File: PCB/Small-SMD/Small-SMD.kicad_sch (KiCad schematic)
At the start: 24 parts, among them J1 Daisy port in, J3 UART, J4 Daisy port out, K1 HYC77-TF09-200, U1 PC817C-S, U2 SE5218, U21 TXB0104QPWRQ1

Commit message: Switch to cheaper IDC box header
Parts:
- J1: LCSC C305958 -> C3405
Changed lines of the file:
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@@
 			)
 		)
-		(property "LCSC" "C305958"
+		(property "LCSC" "C3405"
 			(at 129.54 36.83 0)
 			(effects

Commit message: Fix D2
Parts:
- D2: LCSC C258170 -> C167101
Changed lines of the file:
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@@
 			)
 		)
-		(property "LCSC" "C258170"
+		(property "LCSC" "C167101"
 			(at 168.91 49.53 90)
 			(effects

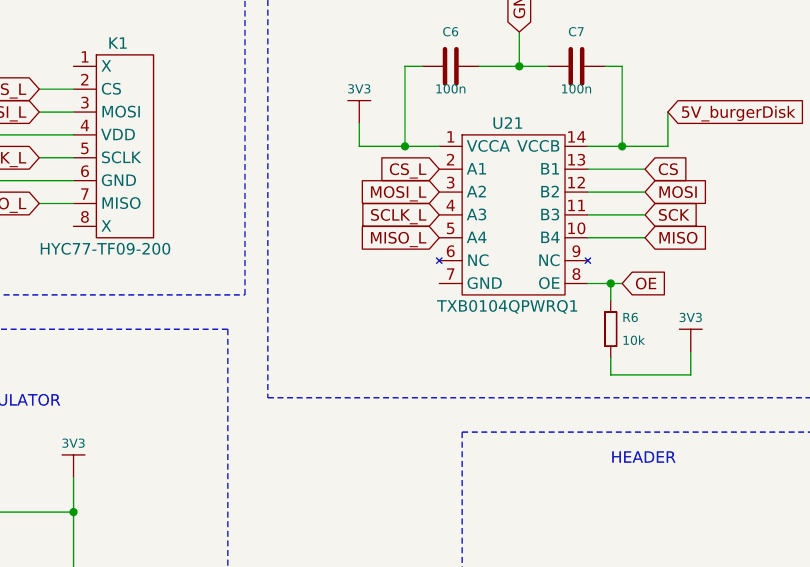
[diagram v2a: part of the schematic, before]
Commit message: Add GND to level shifter :-/
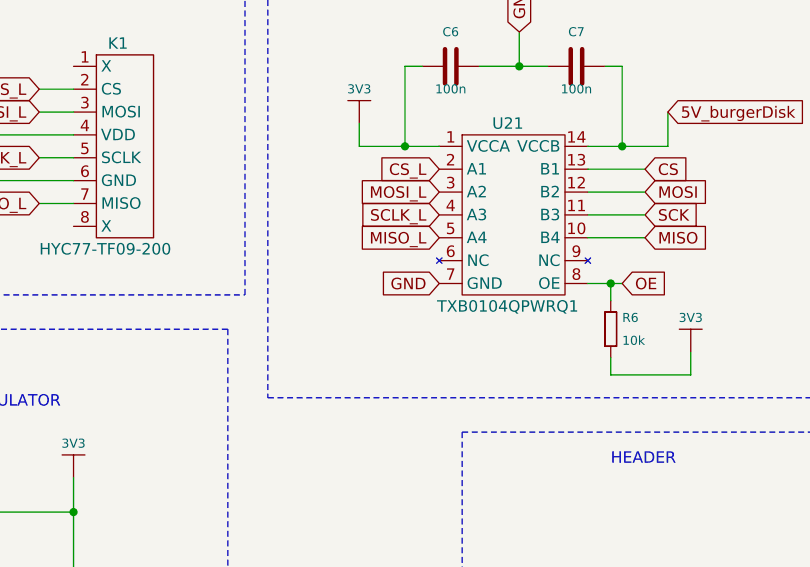
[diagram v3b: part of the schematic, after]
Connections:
- net GND: now also U21.7 (GND)
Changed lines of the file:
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@@
+		)
+	)
+	(global_label "GND"
+		(shape input)
+		(at -50.8 55.88 180)
+		(fields_autoplaced yes)
+		(effects
+			(font
+				(size 1.27 1.27)
+			)
+			(justify right)
+		)
+		(property "Intersheetrefs" "${INTERSHEET_REFS}"
+			(at -57.6557 55.88 0)
+			(effects
+				(font
+					(size 1.27 1.27)
+				)
+				(justify right)
+				(hide yes)
+			)
 		)
 	)

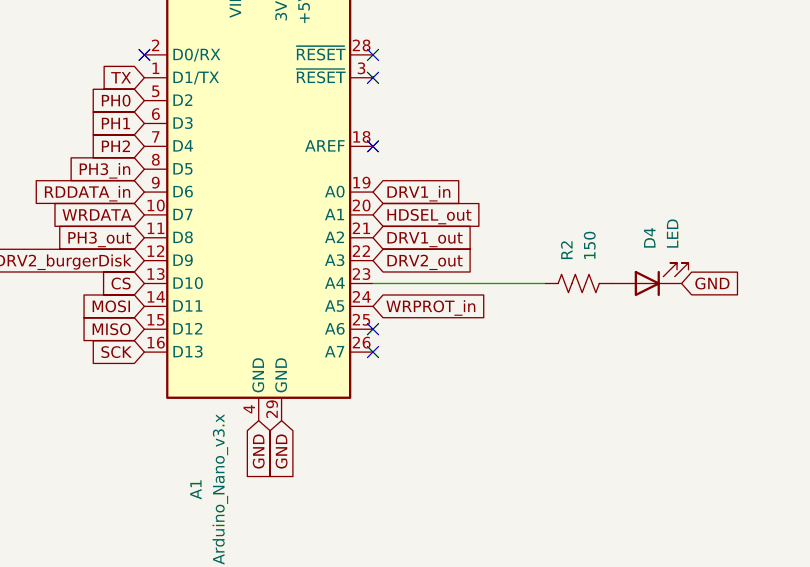
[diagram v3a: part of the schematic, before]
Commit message: WIP untested very small PCB
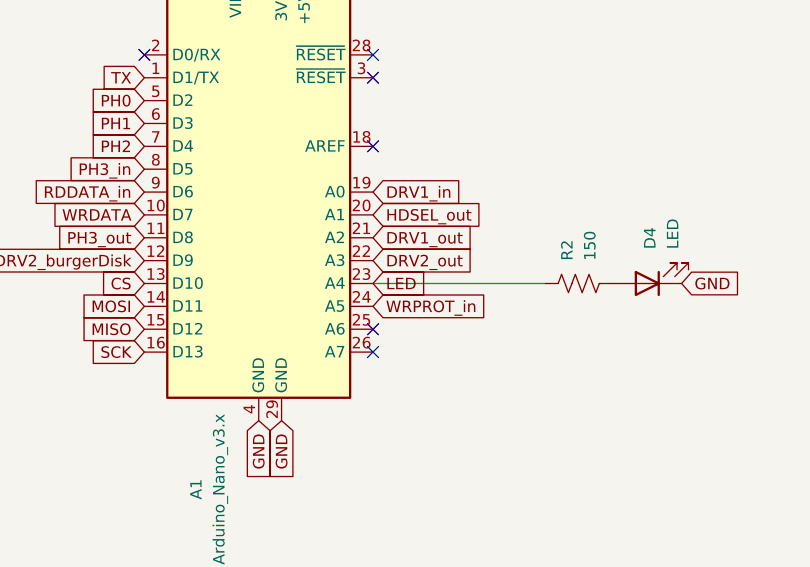
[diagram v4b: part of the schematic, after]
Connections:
- net LED: now reaches A1.23 (A4), R2.2
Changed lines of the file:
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@@
+		)
+	)
+	(global_label "LED"
+		(shape input)
+		(at 165.1 113.03 0)
+		(fields_autoplaced yes)
+		(effects
+			(font
+				(size 1.27 1.27)
+			)
+			(justify left)
+		)
+		(property "Intersheetrefs" "${INTERSHEET_REFS}"
+			(at 171.5323 113.03 0)
+			(effects
+				(font
+					(size 1.27 1.27)
+				)
+				(justify left)
+				(hide yes)
+			)
 		)
 	)
